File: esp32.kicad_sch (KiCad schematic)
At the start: 28 parts, among them J1 Conn_01x02_Pin, J3 Conn_01x03_Pin, Q1 BSS138, Q2 BSS138, U1 ESP32-WROOM-32UE, U2 CH340C

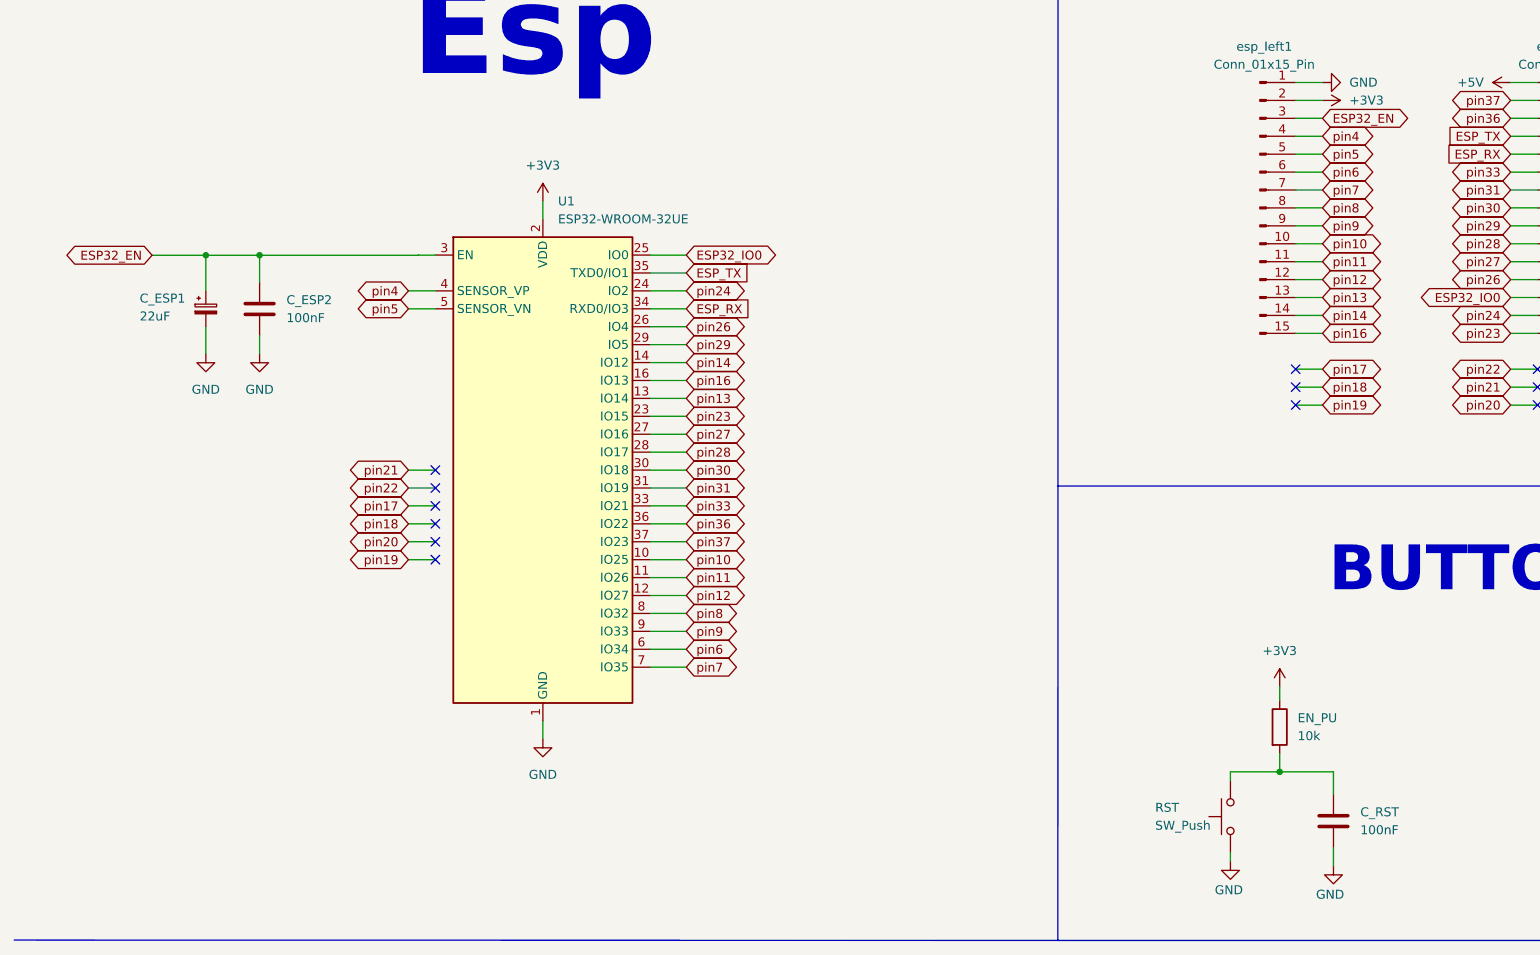
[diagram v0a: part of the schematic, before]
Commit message: removed c at processor
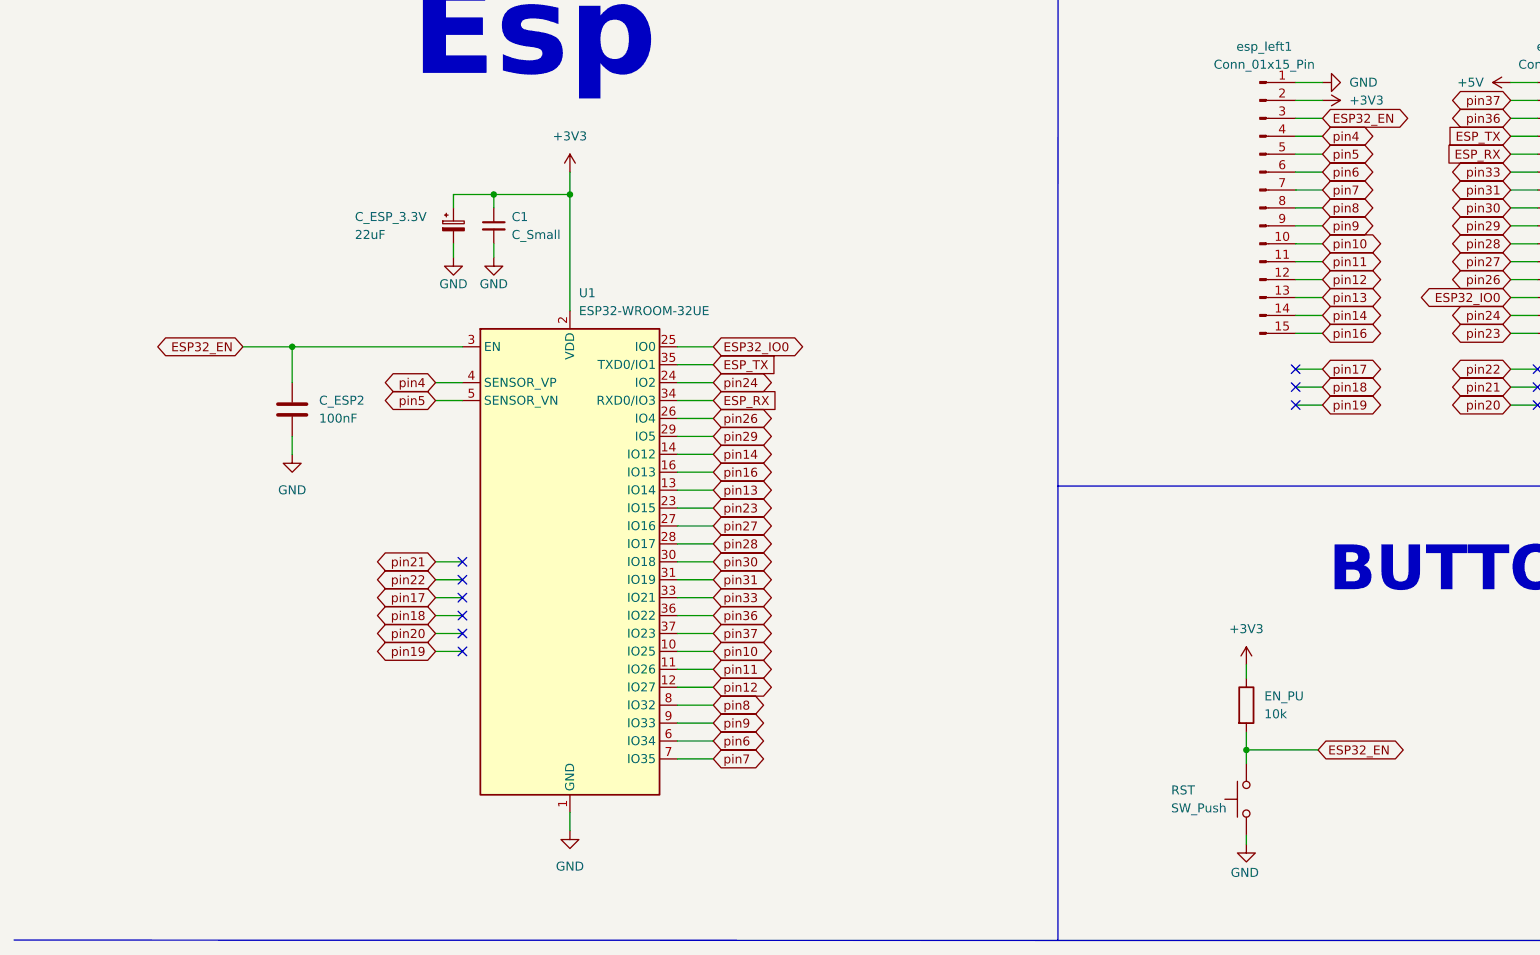
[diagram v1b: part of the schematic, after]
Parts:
- removed C_ESP1: 22uF, Capacitor_SMD:CP_Elec_5x5.4, symbol Device:C_Polarized_Small
- removed C_RST: 100nF, Capacitor_SMD:C_0805_2012Metric_Pad1.18x1.45mm_HandSolder, symbol Device:C
- added C1: C_Small, symbol Device:C_Small
- added C_ESP_3.3V: 22uF, Capacitor_SMD:CP_Elec_5x5.4, symbol Device:C_Polarized_Small
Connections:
- net +3V3: now also C1.1, C_ESP_3.3V.1
- net ESP32_EN: now also EN_PU.2, RST.2
- net GND: now also C1.2, C_ESP_3.3V.2
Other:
- moved on the sheet: C_ESP2, EN_PU, RST, U1
